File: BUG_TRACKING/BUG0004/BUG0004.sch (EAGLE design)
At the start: 1 part

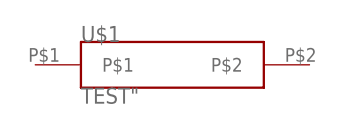
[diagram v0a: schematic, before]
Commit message: Created worst case part to test bug
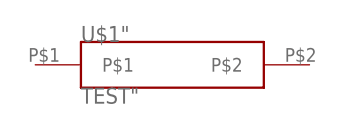
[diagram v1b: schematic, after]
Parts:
- renumbered U$1 to U$1"
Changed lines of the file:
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@@
 </classes>
 <parts>
-<part name="U$1" library="test_doublequote" deviceset="TEST" device="" value="TEST&quot;"/>
+<part name="U$1&quot;" library="test_doublequote" deviceset="TEST" device="" value="TEST&quot;"/>
 </parts>
 <sheets>
@@
 </plain>
 <instances>
-<instance part="U$1" gate="G$1" x="12.7" y="17.78">
+<instance part="U$1&quot;" gate="G$1" x="12.7" y="17.78">
 <attribute name="NAME" x="2.54" y="20.32" size="1.778" layer="95"/>
 <attribute name="VALUE" x="2.54" y="15.24" size="1.778" layer="96" rot="MR180"/>
